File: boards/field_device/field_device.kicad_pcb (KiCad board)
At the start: 4 copper layers, 51 parts, among them J1 Conn_01x05_Pin, J2 Conn_01x02_Pin, SW1 SW_SPST, U1 CHT20MEMS, U2 STM32C011F6Px, U3 SPA06-003, U4 CN3163, U5 HX8001-AJC, U6 SX1262IMLTRT, Y1 Crystal_GND24

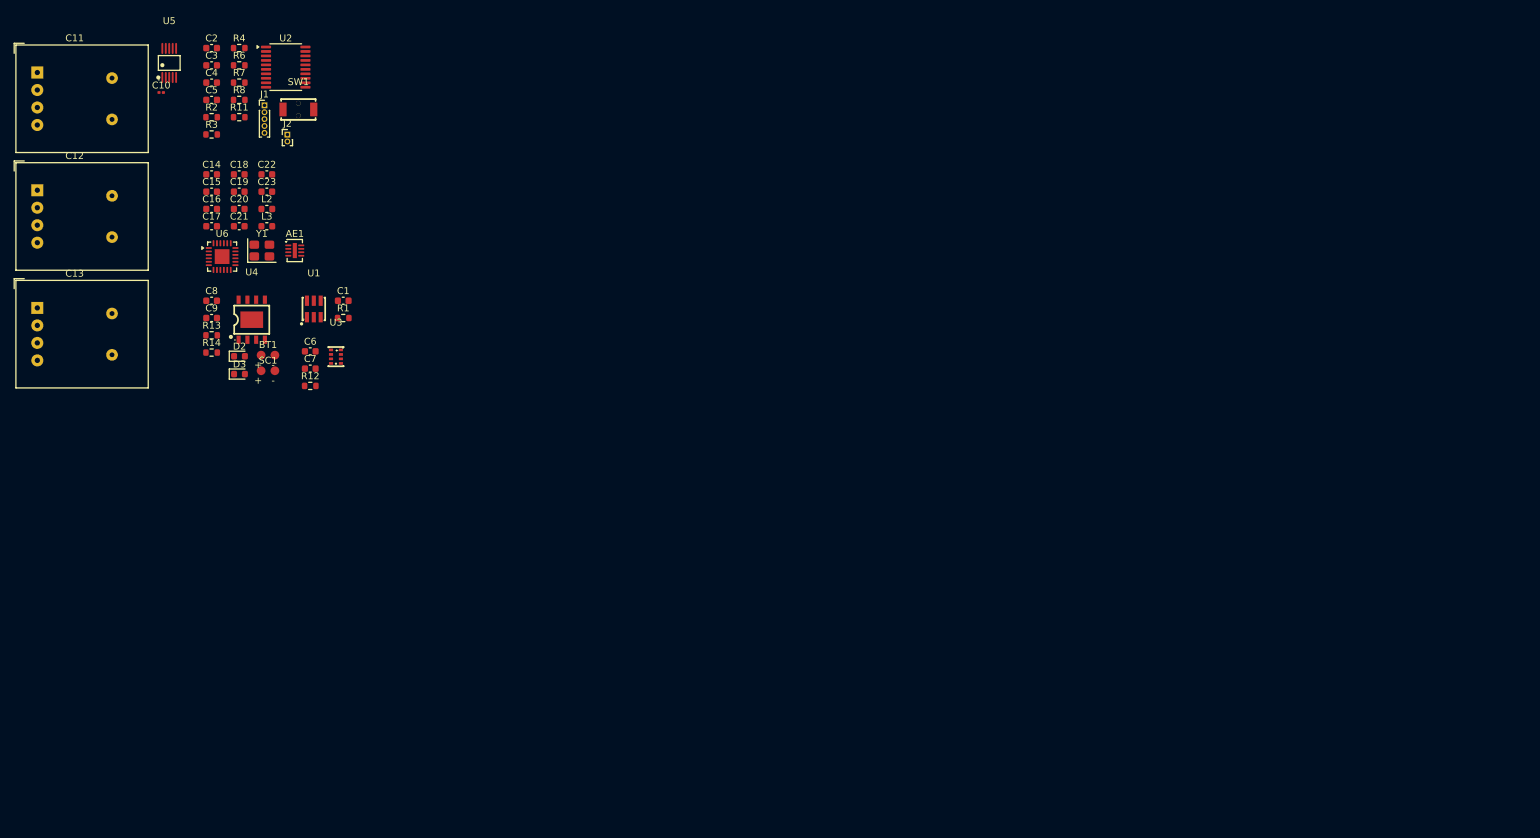
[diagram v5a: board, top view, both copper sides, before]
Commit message: assigned better footprints
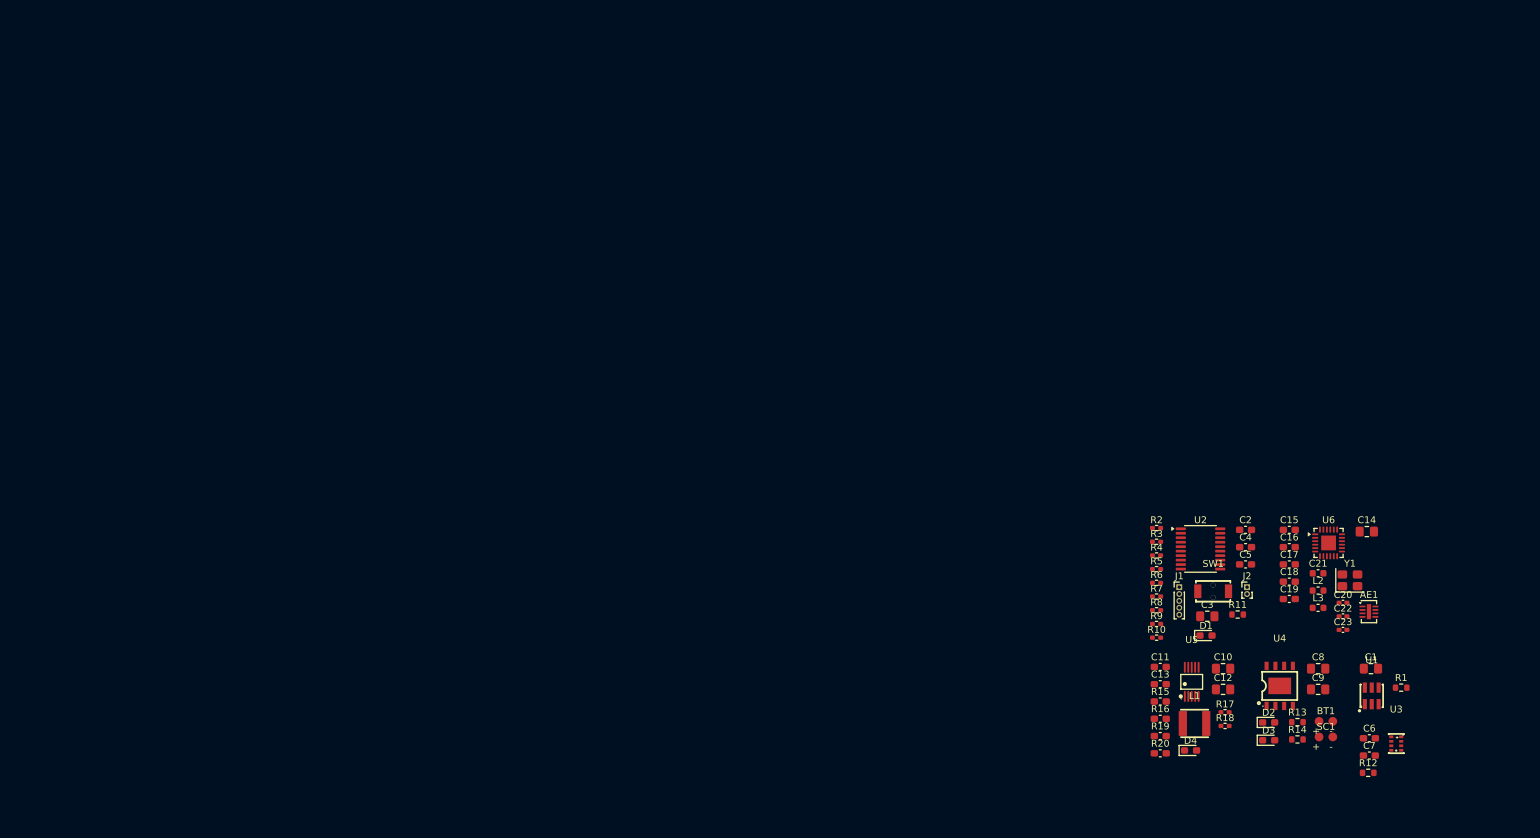
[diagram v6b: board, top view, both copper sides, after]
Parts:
- added D1: STATUS, LED_SMD:LED_0603_1608Metric_Pad1.05x0.95mm_HandSolder, F.Cu at (173.2, 86.1)
- added D4: PWR, LED_SMD:LED_0603_1608Metric_Pad1.05x0.95mm_HandSolder, F.Cu at (170.9, 102.8)
- added L1: 10u, UnEasy-LCSC:IND-SMD_L4.0-W4.0_B, F.Cu at (171.5, 98.9)
- added R10: 10k, Resistor_SMD:R_0402_1005Metric_Pad0.72x0.64mm_HandSolder, F.Cu at (166.0, 86.4)
- added R15: 1M, Capacitor_SMD:C_0603_1608Metric_Pad1.08x0.95mm_HandSolder, F.Cu at (166.5, 95.7)
- added R16: 10k, Capacitor_SMD:C_0603_1608Metric_Pad1.08x0.95mm_HandSolder, F.Cu at (166.5, 98.2)
- added R17: 340k, Resistor_SMD:R_0402_1005Metric_Pad0.72x0.64mm_HandSolder, F.Cu at (175.9, 97.2)
- added R18: 200k, Resistor_SMD:R_0402_1005Metric_Pad0.72x0.64mm_HandSolder, F.Cu at (175.9, 99.2)
- added R19: 15k, Capacitor_SMD:C_0603_1608Metric_Pad1.08x0.95mm_HandSolder, F.Cu at (166.5, 100.7)
- added R20: 60k4, Capacitor_SMD:C_0603_1608Metric_Pad1.08x0.95mm_HandSolder, F.Cu at (166.5, 103.2)
- added R5: 22R, Resistor_SMD:R_0402_1005Metric_Pad0.72x0.64mm_HandSolder, F.Cu at (166.0, 76.4)
- added R9: 1k, Resistor_SMD:R_0402_1005Metric_Pad0.72x0.64mm_HandSolder, F.Cu at (166.0, 84.4)
- C1, C14, C3: footprint Capacitor_SMD:C_0603_1608Metric -> Capacitor_SMD:C_0805_2012Metric_Pad1.18x1.45mm_HandSolder
- C10: footprint Capacitor_SMD:C_0201_0603Metric -> Capacitor_SMD:C_0805_2012Metric_Pad1.18x1.45mm_HandSolder
- C11, C13: footprint Sensor_Current:LEM_HX02-P -> Capacitor_SMD:C_0603_1608Metric_Pad1.08x0.95mm_HandSolder
- C12: footprint Sensor_Current:LEM_HX02-P -> Capacitor_SMD:C_0805_2012Metric_Pad1.18x1.45mm_HandSolder
- C15, C16, C17, C18, C19, C2, C4, C5, C6, C7: footprint Capacitor_SMD:C_0603_1608Metric -> Capacitor_SMD:C_0603_1608Metric_Pad1.08x0.95mm_HandSolder
- C20, C22, C23: footprint Capacitor_SMD:C_0603_1608Metric -> Capacitor_SMD:C_0402_1005Metric_Pad0.74x0.62mm_HandSolder
- C8, C9: value 1u -> 10u; footprint Capacitor_SMD:C_0603_1608Metric -> Capacitor_SMD:C_0805_2012Metric_Pad1.18x1.45mm_HandSolder
- D2, D3: footprint LED_SMD:LED_0603_1608Metric -> LED_SMD:LED_0603_1608Metric_Pad1.05x0.95mm_HandSolder
- R13: value 1kΩ -> 1k5
- R14: value 1k5 -> 1kΩ
- R2, R3, R4, R6, R7: footprint Resistor_SMD:R_0603_1608Metric -> Resistor_SMD:R_0402_1005Metric_Pad0.72x0.64mm_HandSolder
- R8: value 22R -> 1k; footprint Resistor_SMD:R_0603_1608Metric -> Resistor_SMD:R_0402_1005Metric_Pad0.72x0.64mm_HandSolder
- moved C12 186.9 mm to (175.6, 93.9)
- moved C11 184.5 mm to (166.5, 90.6)
- moved C14 175.6 mm to (196.5, 71.0)
- moved C10 175.5 mm to (175.6, 90.9)
- moved U5 173.6 mm to (171.1, 92.8)
- moved C13 172.0 mm to (166.5, 93.2)
- moved C20 170.2 mm to (193.1, 81.3)
- moved C9 169.5 mm to (189.5, 93.9)
- moved C8 169.4 mm to (189.5, 90.9)
- moved C22 169.0 mm to (193.1, 83.3)
- moved C23 168.8 mm to (193.1, 85.3)
- moved R13 167.4 mm to (186.4, 98.7)
- moved R14 167.4 mm to (186.4, 101.2)
- moved U6 166.0 mm to (191.0, 72.6)
- moved C2 165.7 mm to (178.9, 70.7)
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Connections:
- R13 pad 1: /power_source/solar_pwr -> Net-(U4-ISET)
- R13 pad 2: Net-(D2-A) -> GND
- R14 pad 1: Net-(U4-ISET) -> /power_source/solar_pwr
- R14 pad 2: GND -> Net-(D2-A)
- R6 pad 1: /MCU/RF_SCK -> /MCU/RF_MISO
- R6 pad 2: /MCU/RF_SCK -> /MCU/RF_MISO
- R7 pad 1: /MCU/RF_MISO -> /MCU/RF_MOSI
- R7 pad 2: /MCU/RF_MISO -> /MCU/RF_MOSI
- R8 pad 1: /MCU/RF_MOSI -> /MCU/LOG_MCU_TX
- R8 pad 2: /MCU/RF_MOSI -> /MCU/LOG_MCU_TX_DEBUGGER_RX
- U2 pad 15: Net-(U2-PA8) -> /MCU/STATUS_LED

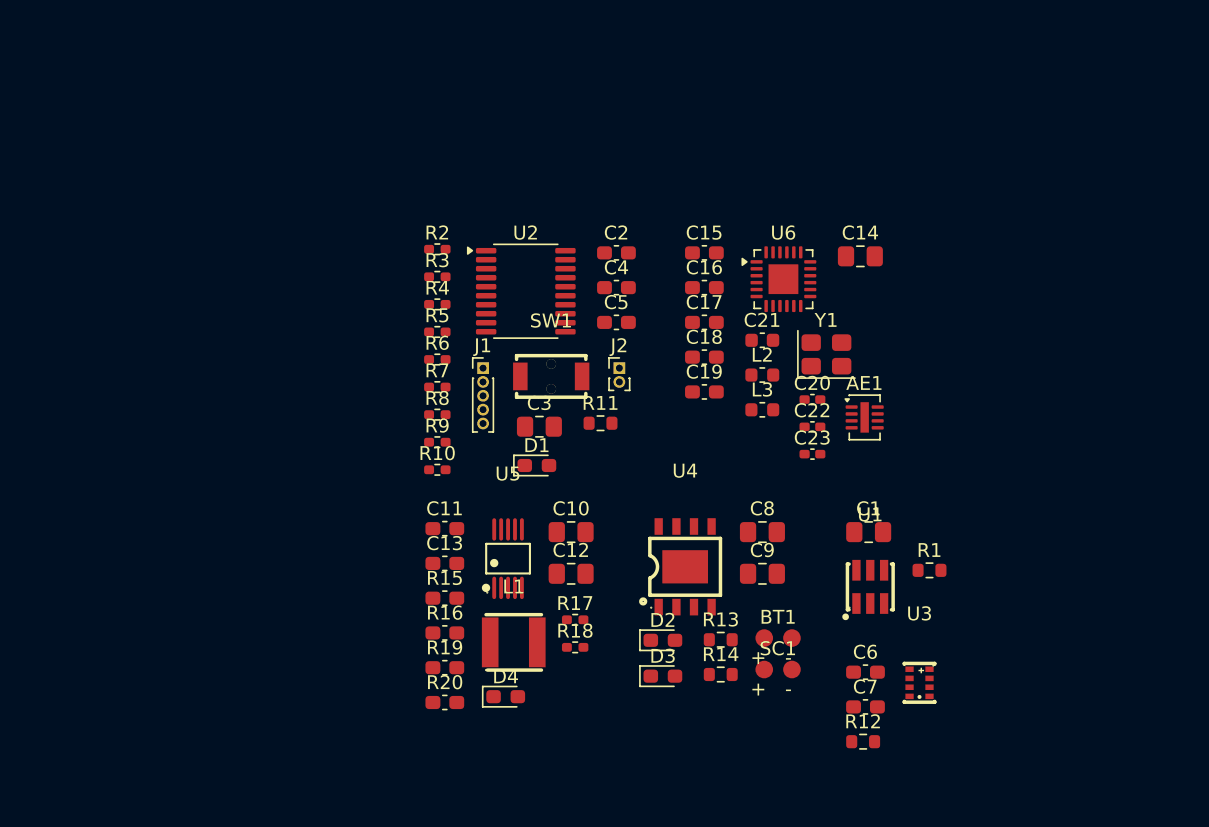
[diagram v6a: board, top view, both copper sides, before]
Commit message: changed regulator
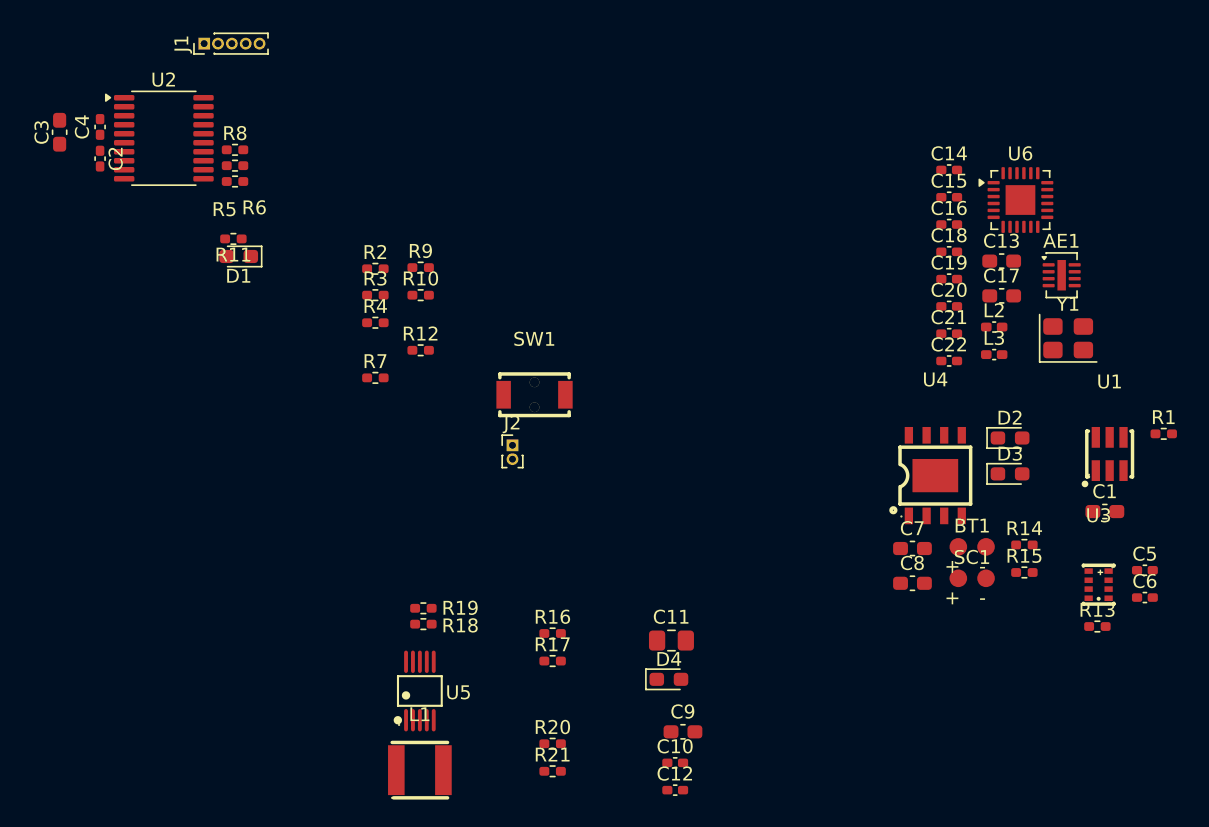
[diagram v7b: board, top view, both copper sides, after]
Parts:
- removed C23: C_Shunt_2, Capacitor_SMD:C_0402_1005Metric_Pad0.74x0.62mm_HandSolder
- added R21: 60k4, Resistor_SMD:R_0402_1005Metric_Pad0.72x0.64mm_HandSolder, F.Cu at (174.3, 108.2)
- C1, C3, C8, C9: footprint Capacitor_SMD:C_0805_2012Metric_Pad1.18x1.45mm_HandSolder -> Capacitor_SMD:C_0603_1608Metric_Pad1.08x0.95mm_HandSolder
- C10: value 10u -> 100n; footprint Capacitor_SMD:C_0805_2012Metric_Pad1.18x1.45mm_HandSolder -> Capacitor_SMD:C_0402_1005Metric_Pad0.74x0.62mm_HandSolder
- C11: value 100n -> 22u; footprint Capacitor_SMD:C_0603_1608Metric_Pad1.08x0.95mm_HandSolder -> Capacitor_SMD:C_0805_2012Metric_Pad1.18x1.45mm_HandSolder
- C12: value 22u -> 1n5; footprint Capacitor_SMD:C_0805_2012Metric_Pad1.18x1.45mm_HandSolder -> Capacitor_SMD:C_0402_1005Metric_Pad0.74x0.62mm_HandSolder
- C13: value 1n5 -> 10uF
- C14: value 10uF -> 100nF; footprint Capacitor_SMD:C_0805_2012Metric_Pad1.18x1.45mm_HandSolder -> Capacitor_SMD:C_0402_1005Metric_Pad0.74x0.62mm_HandSolder
- C15, C16, C2, C4, C5, C6: footprint Capacitor_SMD:C_0603_1608Metric_Pad1.08x0.95mm_HandSolder -> Capacitor_SMD:C_0402_1005Metric_Pad0.74x0.62mm_HandSolder
- C17: value 100nF -> 470nF
- C18: value 470nF -> 47nF; footprint Capacitor_SMD:C_0603_1608Metric_Pad1.08x0.95mm_HandSolder -> Capacitor_SMD:C_0402_1005Metric_Pad0.74x0.62mm_HandSolder
- C19: value 47nF -> 100pF; footprint Capacitor_SMD:C_0603_1608Metric_Pad1.08x0.95mm_HandSolder -> Capacitor_SMD:C_0402_1005Metric_Pad0.74x0.62mm_HandSolder
- C21: value 100pF -> C_Shunt_1; footprint Capacitor_SMD:C_0603_1608Metric -> Capacitor_SMD:C_0402_1005Metric_Pad0.74x0.62mm_HandSolder
- C22: value C_Shunt_1 -> C_Shunt_2
- C7: value 100n -> 10u
- L2, L3: footprint Inductor_SMD:L_0603_1608Metric -> Inductor_SMD:L_0402_1005Metric_Pad0.77x0.64mm_HandSolder
- R1, R11: footprint Resistor_SMD:R_0603_1608Metric -> Resistor_SMD:R_0402_1005Metric_Pad0.72x0.64mm_HandSolder
- R10: value 10k -> 1k
- R12: value 10k? -> 10k; footprint Resistor_SMD:R_0603_1608Metric -> Resistor_SMD:R_0402_1005Metric_Pad0.72x0.64mm_HandSolder
- R13: value 1k5 -> 10k?; footprint Resistor_SMD:R_0603_1608Metric -> Resistor_SMD:R_0402_1005Metric_Pad0.72x0.64mm_HandSolder
- R14: value 1kΩ -> 1k5; footprint Resistor_SMD:R_0603_1608Metric -> Resistor_SMD:R_0402_1005Metric_Pad0.72x0.64mm_HandSolder
- R15: value 1M -> 1k; footprint Capacitor_SMD:C_0603_1608Metric_Pad1.08x0.95mm_HandSolder -> Resistor_SMD:R_0402_1005Metric_Pad0.72x0.64mm_HandSolder
- R16: value 10k -> 1M; footprint Capacitor_SMD:C_0603_1608Metric_Pad1.08x0.95mm_HandSolder -> Resistor_SMD:R_0402_1005Metric_Pad0.72x0.64mm_HandSolder
- R17: value 340k -> 10k
- R18: value 200k -> 340k
- R19: value 15k -> 200k; footprint Capacitor_SMD:C_0603_1608Metric_Pad1.08x0.95mm_HandSolder -> Resistor_SMD:R_0402_1005Metric_Pad0.72x0.64mm_HandSolder
- R20: value 60k4 -> 15k; footprint Capacitor_SMD:C_0603_1608Metric_Pad1.08x0.95mm_HandSolder -> Resistor_SMD:R_0402_1005Metric_Pad0.72x0.64mm_HandSolder
- R8: value 1k -> 22R
- moved C13 45.7 mm to (206.7, 71.3)
- moved R12 42.6 mm to (164.8, 77.8)
- moved C5 42.1 mm to (217.1, 93.6)
- moved R15 41.9 mm to (208.4, 93.8)
- moved C3 40.6 mm to (138.7, 62.0), turned to -90 degrees
- moved C4 39.0 mm to (141.6, 61.6), turned to -90 degrees
- moved C2 37.9 mm to (141.6, 63.9), turned to -90 degrees
- moved J1 30.9 mm to (149.1, 55.6), turned to 90 degrees
- moved R11 29.7 mm to (151.3, 69.7), turned to 180 degrees
- moved D2 29.0 mm to (207.3, 84.1)
- moved D3 29.0 mm to (207.3, 86.7)
- moved U2 28.4 mm to (146.2, 62.5)
- moved R13 27.2 mm to (213.6, 97.7)
- moved D1 26.3 mm to (151.6, 71.0), turned to 180 degrees
- moved R8 24.1 mm to (151.4, 63.3)
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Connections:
- C10 pad 1: VBUS -> /power_source/regulator/EN
- C11 pad 1: /power_source/regulator/EN -> +3.3V
- C12 pad 1: +3.3V -> Net-(C12-Pad1)
- C12 pad 2: GND -> Net-(U5-VC)
- C13 pad 1: Net-(C13-Pad1) -> +3.3V
- C13 pad 2: Net-(U5-VC) -> GND
- C17 pad 1: +3.3V -> Net-(U6-VREG)
- C18 pad 1: Net-(U6-VREG) -> Net-(U6-VR_PA)
- C20 pad 1: Net-(U6-VR_PA) -> Net-(C20-Pad1)
- C20 pad 2: GND -> Net-(U6-RFO)
- C21 pad 1: Net-(C21-Pad1) -> Net-(C20-Pad1)
- C21 pad 2: Net-(U6-RFO) -> GND
- C22 pad 1: Net-(C21-Pad1) -> Net-(AE1-A)
- C7 pad 1: +3.3V -> /power_source/solar_pwr
- C8 pad 1: /power_source/solar_pwr -> VBUS
- L3 pad 1: Net-(C21-Pad1) -> Net-(C20-Pad1)
- R10 pad 1: /MCU/STATUS_LED -> /MCU/LOG_MCU_RX
- R10 pad 2: Net-(D1-A) -> /MCU/LOG_MCU_RX_DEBUGGER_TX
- R11 pad 1: /MCU/RF_NSS -> /MCU/STATUS_LED
- R11 pad 2: +3.3V -> Net-(D1-A)
- R12 pad 1: +3.3V -> /MCU/RF_NSS
- R12 pad 2: Net-(U3-CSB) -> +3.3V
- R13 pad 1: Net-(U4-ISET) -> +3.3V
- R13 pad 2: GND -> Net-(U3-CSB)
- R14 pad 1: /power_source/solar_pwr -> Net-(U4-ISET)
- R14 pad 2: Net-(D2-A) -> GND
- R15 pad 1: /power_source/regulator/EN -> /power_source/solar_pwr
- R15 pad 2: VBUS -> Net-(D2-A)
- R16 pad 1: +3.3V -> /power_source/regulator/EN
- R16 pad 2: Net-(D4-A) -> VBUS
- R17 pad 2: /power_source/regulator/FB_NETWORK -> Net-(D4-A)
- R18 pad 1: /power_source/regulator/FB_NETWORK -> +3.3V
- R18 pad 2: GND -> /power_source/regulator/FB_NETWORK
- R19 pad 2: Net-(C13-Pad1) -> GND
- R20 pad 1: /power_source/regulator/RT -> /power_source/regulator/FB_NETWORK
- R20 pad 2: GND -> Net-(C12-Pad1)
- R5 pad 1: /MCU/RF_SCK -> /MCU/RF_NSS
- R5 pad 2: /MCU/RF_SCK -> /MCU/RF_NSS
- R6 pad 1: /MCU/RF_MISO -> /MCU/RF_SCK
- R6 pad 2: /MCU/RF_MISO -> /MCU/RF_SCK
- R7 pad 1: /MCU/RF_MOSI -> /MCU/RF_MISO
- R7 pad 2: /MCU/RF_MOSI -> /MCU/RF_MISO
- R8 pad 1: /MCU/LOG_MCU_TX -> /MCU/RF_MOSI
- R8 pad 2: /MCU/LOG_MCU_TX_DEBUGGER_RX -> /MCU/RF_MOSI
- R9 pad 1: /MCU/LOG_MCU_RX -> /MCU/LOG_MCU_TX
- R9 pad 2: /MCU/LOG_MCU_RX_DEBUGGER_TX -> /MCU/LOG_MCU_TX_DEBUGGER_RX
